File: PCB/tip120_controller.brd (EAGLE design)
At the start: 52.4 x 37.5 mm, 14 parts, among them J1 AUDIO_JACK_3.5MM_PTH, Q1 TIP120, U1 ARDUINO_MINI

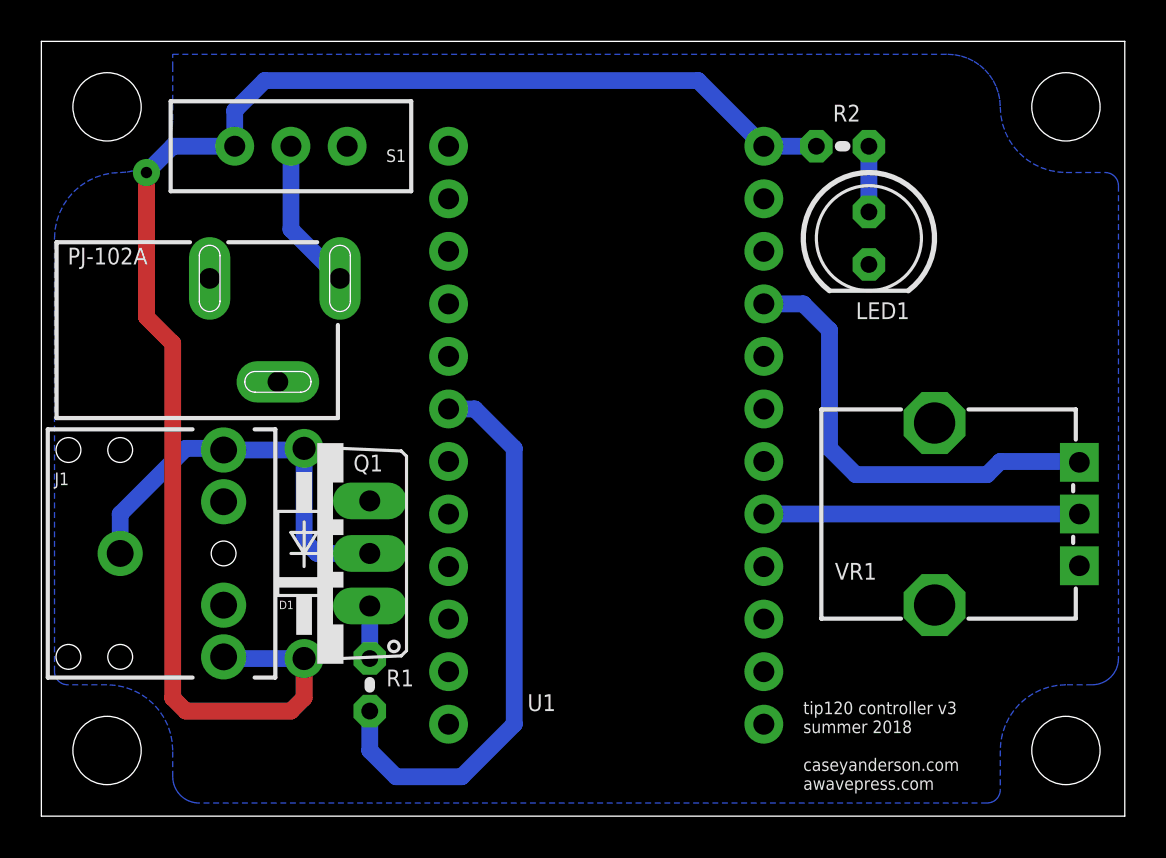
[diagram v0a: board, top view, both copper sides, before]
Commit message: swap footprints, update version number
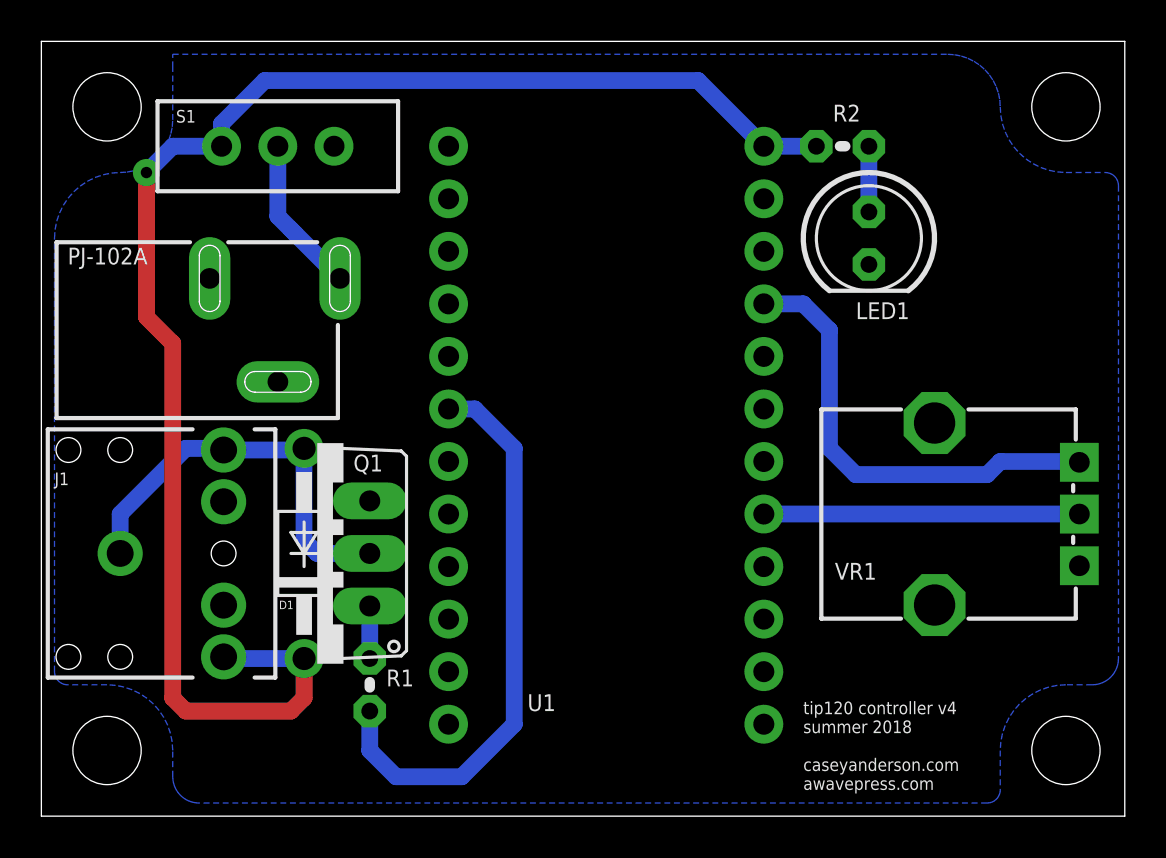
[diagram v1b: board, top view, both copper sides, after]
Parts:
- S1: device SparkFun-Switches:SWITCH_SPDT_PTH_11.6X4.0MM_KIT -> SparkFun-Switches:SWITCH_SPDT_PTH_11.6X4.0MM_LOCK
- moved S1 0.63 mm to (10.8, 78.7)
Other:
- board text added: "tip120 controller v4 summer 2018 caseyanderson.com awavepress.com"
- board text removed: "tip120 controller v3 summer 2018 caseyanderson.com awavepress.com"
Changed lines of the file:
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@@
 <?xml version="1.0" encoding="utf-8"?>
 <!DOCTYPE eagle SYSTEM "eagle.dtd">
-<eagle version="9.0.0">
+<eagle version="9.0.1">
 <drawing>
 <settings>
@@
 <wire x1="51.74" y1="83.81" x2="-0.635" y2="83.81" width="0" layer="20"/>
 <wire x1="-0.635" y1="83.81" x2="-0.635" y2="46.355" width="0" layer="20"/>
-<text x="36.195" y="47.625" size="0.6096" layer="21" font="vector" ratio="15">tip120 controller v3
+<text x="36.195" y="47.625" size="0.6096" layer="21" font="vector" ratio="15">tip120 controller v4
 summer 2018
 caseyanderson.com
@@
 <attribute name="NAME" x="15.875" y="63.8302" size="0.8128" layer="25" font="vector" ratio="15" rot="R180"/>
 </element>
-<element name="S1" library="SparkFun-Switches" package="SWITCH_SPDT_PTH_11.6X4.0MM_KIT" value="EG1218" x="11.43" y="78.74" smashed="yes" rot="R270">
-<attribute name="NAME" x="16.51" y="77.978" size="0.6096" layer="25" font="vector" ratio="20" align="bottom-center"/>
-<attribute name="PROD_ID" value="SWCH-08261" x="11.43" y="78.74" size="1.778" layer="27" rot="R270" display="off"/>
-<attribute name="SF_SKU" value="COM-00102" x="11.43" y="78.74" size="1.778" layer="27" rot="R270" display="off"/>
-<attribute name="VALUE" x="15.24" y="77.597" size="0.6096" layer="27" font="vector" ratio="20" align="top-center"/>
+<element name="S1" library="SparkFun-Switches" package="SWITCH_SPDT_PTH_11.6X4.0MM_LOCK" value="EG1218" x="10.795" y="78.74" smashed="yes" rot="R270">
+<attribute name="NAME" x="6.35" y="79.883" size="0.6096" layer="25" font="vector" ratio="20" align="bottom-center"/>
+<attribute name="PROD_ID" value="SWCH-08261" x="10.795" y="78.74" size="1.778" layer="27" rot="R270" display="off"/>
+<attribute name="SF_SKU" value="COM-00102 " x="10.795" y="78.74" size="1.778" layer="27" rot="R270" display="off"/>
+<attribute name="VALUE" x="6.985" y="77.597" size="0.6096" layer="27" font="vector" ratio="20" align="top-center"/>
 </element>
 </elements>
@@
 <signal name="N$7">
 <contactref element="PJ-102A" pad="1"/>
-<wire x1="13.8" y1="72.35" x2="11.43" y2="74.72" width="0.8128" layer="16"/>
+<wire x1="13.8" y1="72.35" x2="11.6425" y2="74.5075" width="0.8128" layer="16"/>
 <contactref element="S1" pad="2"/>
-<wire x1="11.43" y1="74.72" x2="11.43" y2="78.74" width="0.8128" layer="16"/>
+<wire x1="11.6425" y1="74.5075" x2="11.43" y2="74.72" width="0.8128" layer="16"/>
+<wire x1="11.43" y1="74.72" x2="10.795" y2="75.355" width="0.8128" layer="16"/>
+<wire x1="10.795" y1="75.355" x2="10.795" y2="78.74" width="0.8128" layer="16"/>
 </signal>
 <signal name="N$8">
@@
 <wire x1="8.175" y1="54.055" x2="8.255" y2="53.975" width="0.8128" layer="16"/>
 <wire x1="8.255" y1="53.975" x2="12.065" y2="53.975" width="0.8128" layer="16"/>
-<wire x1="8.7122" y1="80.4672" x2="10.16" y2="81.915" width="0.8128" layer="16"/>
 <wire x1="10.16" y1="81.915" x2="31.115" y2="81.915" width="0.8128" layer="16"/>
 <wire x1="31.115" y1="81.915" x2="34.29" y2="78.74" width="0.8128" layer="16"/>
@@
 <wire x1="4.445" y1="77.47" x2="5.715" y2="78.74" width="0.8128" layer="16"/>
 <contactref element="S1" pad="3"/>
-<wire x1="5.715" y1="78.74" x2="8.7122" y2="78.74" width="0.8128" layer="16"/>
-<wire x1="8.7122" y1="78.74" x2="8.7122" y2="80.4672" width="0.8128" layer="16"/>
+<wire x1="5.715" y1="78.74" x2="8.0772" y2="78.74" width="0.8128" layer="16"/>
+<wire x1="8.0772" y1="78.74" x2="8.0772" y2="79.8322" width="0.8128" layer="16"/>
+<wire x1="8.0772" y1="79.8322" x2="10.16" y2="81.915" width="0.8128" layer="16"/>
 </signal>
 <signal name="N$1">

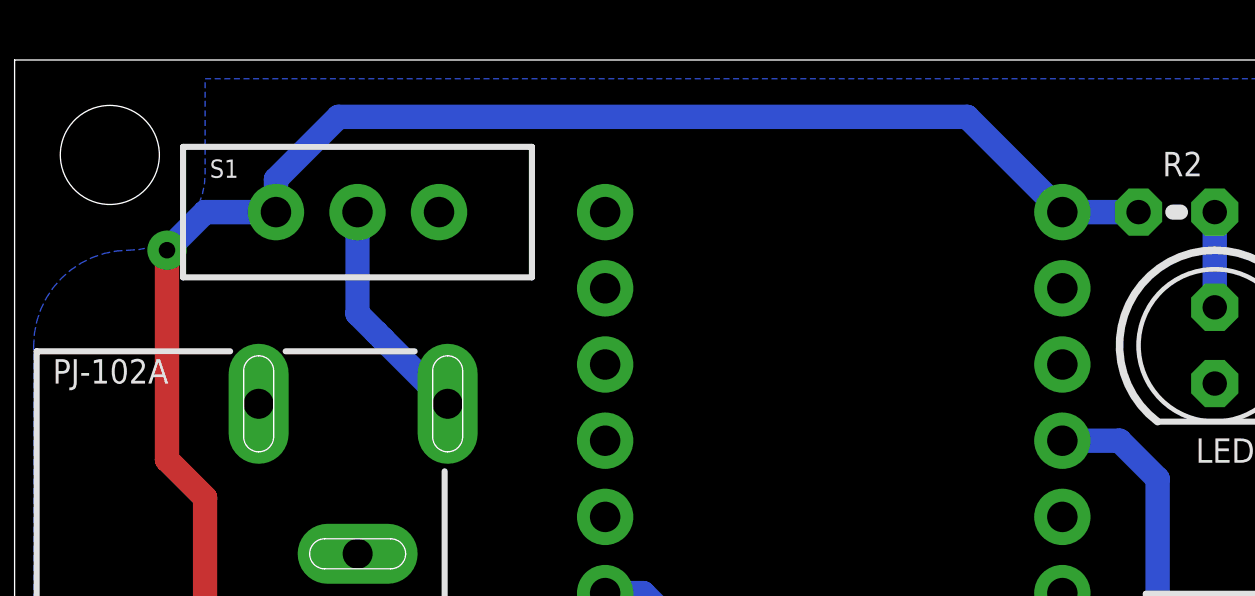
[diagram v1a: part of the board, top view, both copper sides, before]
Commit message: reposition switch
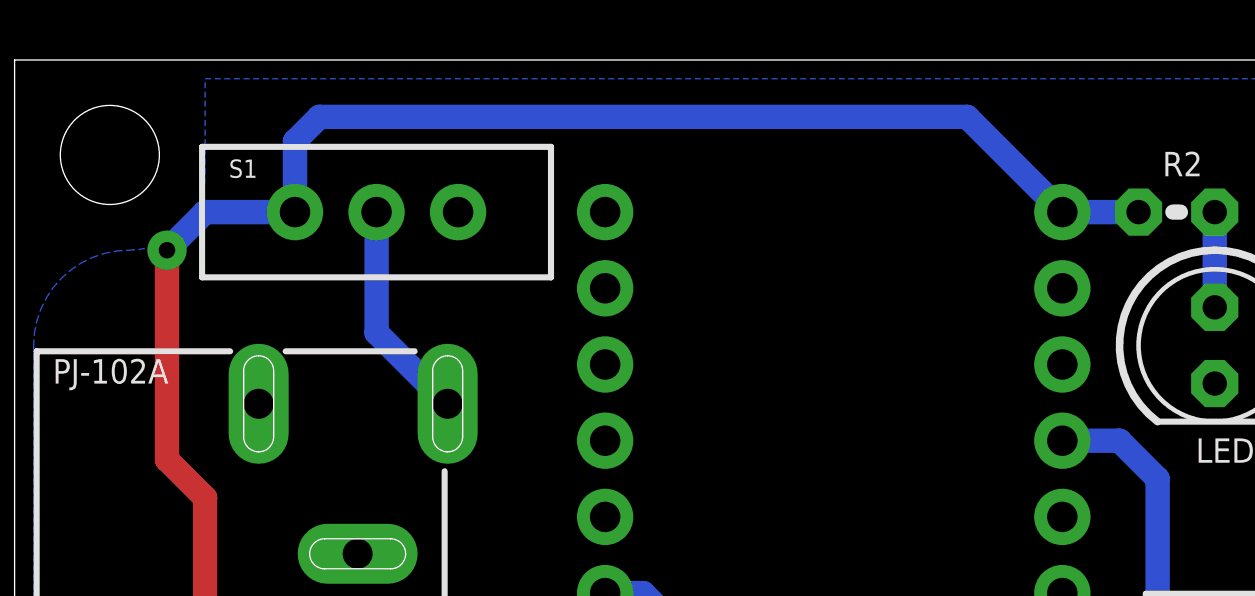
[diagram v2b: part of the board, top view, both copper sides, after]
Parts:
- moved S1 0.63 mm to (11.4, 78.7)
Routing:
- net N$8: track 74.8 -> 75.6 mm
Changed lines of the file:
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@@
 <attribute name="NAME" x="15.875" y="63.8302" size="0.8128" layer="25" font="vector" ratio="15" rot="R180"/>
 </element>
-<element name="S1" library="SparkFun-Switches" package="SWITCH_SPDT_PTH_11.6X4.0MM_LOCK" value="EG1218" x="10.795" y="78.74" smashed="yes" rot="R270">
-<attribute name="NAME" x="6.35" y="79.883" size="0.6096" layer="25" font="vector" ratio="20" align="bottom-center"/>
-<attribute name="PROD_ID" value="SWCH-08261" x="10.795" y="78.74" size="1.778" layer="27" rot="R270" display="off"/>
-<attribute name="SF_SKU" value="COM-00102 " x="10.795" y="78.74" size="1.778" layer="27" rot="R270" display="off"/>
-<attribute name="VALUE" x="6.985" y="77.597" size="0.6096" layer="27" font="vector" ratio="20" align="top-center"/>
+<element name="S1" library="SparkFun-Switches" package="SWITCH_SPDT_PTH_11.6X4.0MM_LOCK" value="EG1218" x="11.43" y="78.74" smashed="yes" rot="R270">
+<attribute name="NAME" x="6.985" y="79.883" size="0.6096" layer="25" font="vector" ratio="20" align="bottom-center"/>
+<attribute name="PROD_ID" value="SWCH-08261" x="11.43" y="78.74" size="1.778" layer="27" rot="R270" display="off"/>
+<attribute name="SF_SKU" value="COM-00102 " x="11.43" y="78.74" size="1.778" layer="27" rot="R270" display="off"/>
+<attribute name="VALUE" x="7.62" y="77.597" size="0.6096" layer="27" font="vector" ratio="20" align="top-center"/>
 </element>
 </elements>
@@
 <signal name="N$7">
 <contactref element="PJ-102A" pad="1"/>
-<wire x1="13.8" y1="72.35" x2="11.6425" y2="74.5075" width="0.8128" layer="16"/>
 <contactref element="S1" pad="2"/>
-<wire x1="11.6425" y1="74.5075" x2="11.43" y2="74.72" width="0.8128" layer="16"/>
-<wire x1="11.43" y1="74.72" x2="10.795" y2="75.355" width="0.8128" layer="16"/>
-<wire x1="10.795" y1="75.355" x2="10.795" y2="78.74" width="0.8128" layer="16"/>
+<wire x1="11.43" y1="78.74" x2="11.43" y2="74.72" width="0.8128" layer="16"/>
+<wire x1="11.43" y1="74.72" x2="13.8" y2="72.35" width="0.8128" layer="16"/>
 </signal>
 <signal name="N$8">
@@
 <wire x1="8.175" y1="54.055" x2="8.255" y2="53.975" width="0.8128" layer="16"/>
 <wire x1="8.255" y1="53.975" x2="12.065" y2="53.975" width="0.8128" layer="16"/>
-<wire x1="10.16" y1="81.915" x2="31.115" y2="81.915" width="0.8128" layer="16"/>
-<wire x1="31.115" y1="81.915" x2="34.29" y2="78.74" width="0.8128" layer="16"/>
+<wire x1="34.29" y1="78.74" x2="31.115" y2="81.915" width="0.8128" layer="16"/>
 <via x="4.445" y="77.47" extent="1-16" drill="0.55" diameter="0.35"/>
 <wire x1="5.715" y1="69.215" x2="5.715" y2="52.07" width="0.8128" layer="1"/>
@@
 <wire x1="4.445" y1="77.47" x2="5.715" y2="78.74" width="0.8128" layer="16"/>
 <contactref element="S1" pad="3"/>
-<wire x1="5.715" y1="78.74" x2="8.0772" y2="78.74" width="0.8128" layer="16"/>
-<wire x1="8.0772" y1="78.74" x2="8.0772" y2="79.8322" width="0.8128" layer="16"/>
-<wire x1="8.0772" y1="79.8322" x2="10.16" y2="81.915" width="0.8128" layer="16"/>
+<wire x1="5.715" y1="78.74" x2="8.7122" y2="78.74" width="0.8128" layer="16"/>
+<wire x1="31.115" y1="81.915" x2="9.525" y2="81.915" width="0.8128" layer="16"/>
+<wire x1="8.7122" y1="81.1022" x2="8.7122" y2="78.74" width="0.8128" layer="16"/>
+<wire x1="9.525" y1="81.915" x2="8.7122" y2="81.1022" width="0.8128" layer="16"/>
 </signal>
 <signal name="N$1">
